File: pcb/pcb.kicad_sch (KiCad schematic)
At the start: 19 parts, among them CN1 1x4, CN10 1x2, CN11 1x2, CN12 1x8, CN2 1x8, CN3 1x8, CN4 1x8, CN5 1x4, CN6 1x2, CN7 1x2, CN8 1x8, SW3 219-3LPST

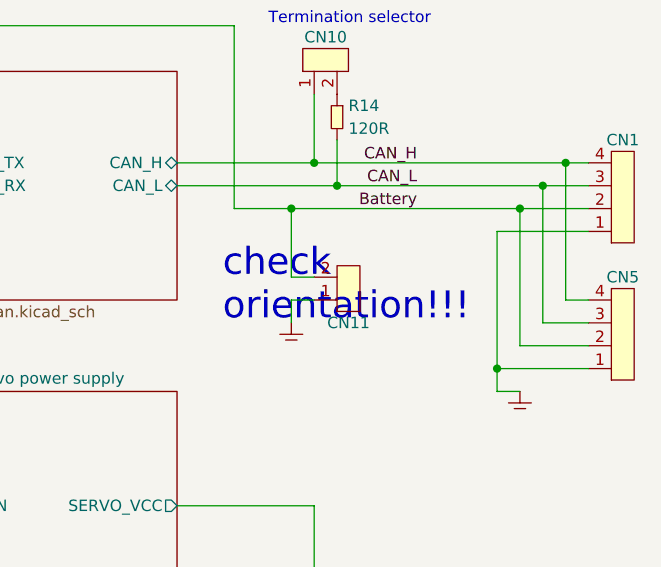
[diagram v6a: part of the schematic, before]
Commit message: changed CAN driver
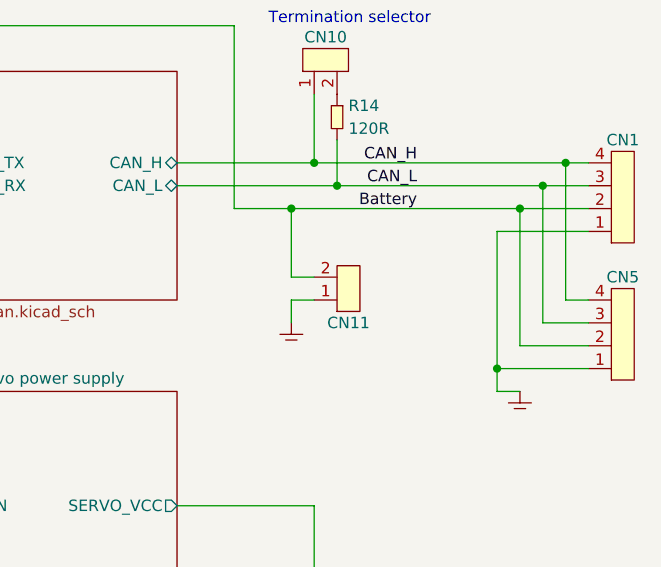
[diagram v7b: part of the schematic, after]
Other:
- note removed: "check orientation!!!"
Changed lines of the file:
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@@
-		)
-	)
-	(text "check\norientation!!!"
-		(exclude_from_sim no)
-		(at 208.28 76.2 0)
-		(effects
-			(font
-				(size 3 3)
-				(color 255 0 56 1)
-			)
-			(justify left bottom)
 		)
 	)
@@
 			(project "pcb"
 				(path "/6bb3bad6-1a89-4624-b34d-6ddda7dd16d2"
-					(page "23")
+					(page "7")
 				)
 			)
@@
 			(project "pcb"
 				(path "/6bb3bad6-1a89-4624-b34d-6ddda7dd16d2"
-					(page "14")
-				)
-			)
+					(page "6")
+				)
+			)
